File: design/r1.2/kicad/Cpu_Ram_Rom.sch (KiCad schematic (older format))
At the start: 19 parts, among them IC1 MC68010P10, IC4 MC68901P, J2 Conn_01x06, Q1 3.6864MHz, U1 AT28C256-15PU, U2 AT28C256-15PU, U3 AS6C4008-55PCN, U4 AS6C4008-55PCN

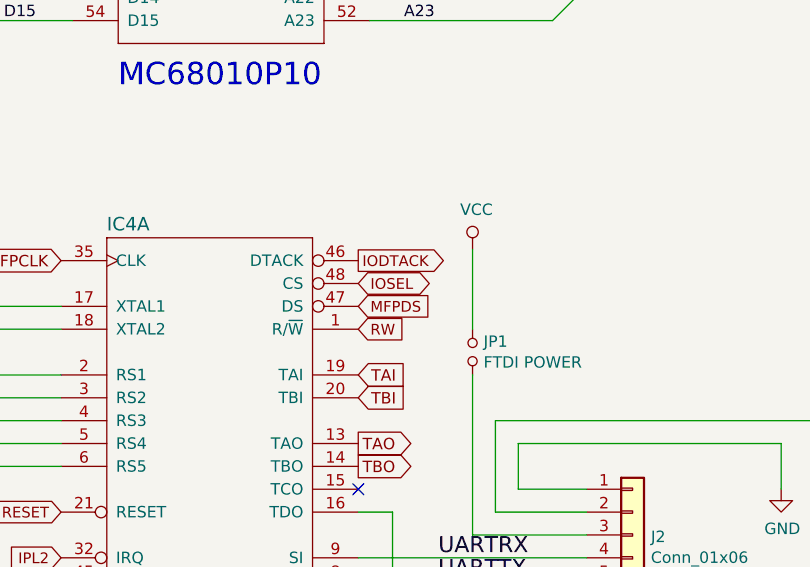
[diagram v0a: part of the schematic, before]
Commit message: More robust MFP decoding
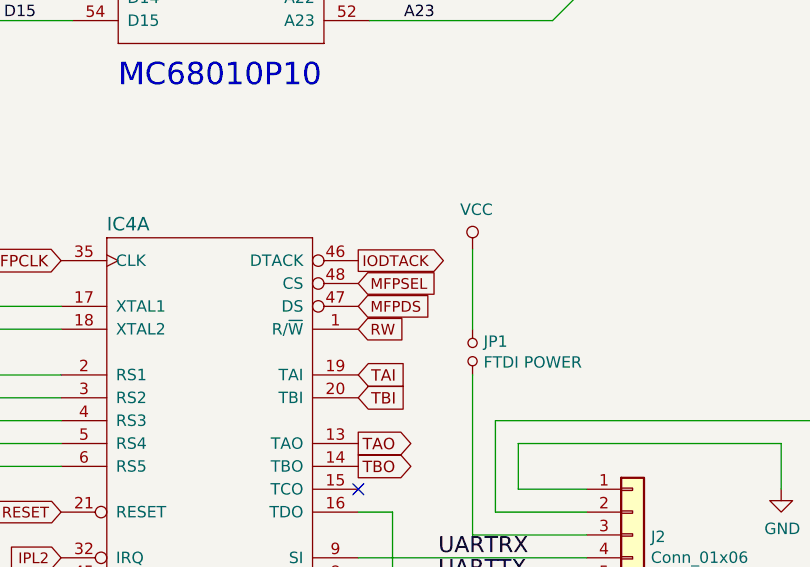
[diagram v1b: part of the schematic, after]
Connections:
- net IOSEL renamed MFPSEL
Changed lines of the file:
@@
 Text GLabel 4000 7550 0    47   Input ~ 0
 RESET
-Text GLabel 5300 6550 2    47   BiDi ~ 0
-IOSEL
+Text GLabel 5300 6550 2    47   Input ~ 0
+MFPSEL
 Wire Wire Line
 	1000 9100 1400 9100

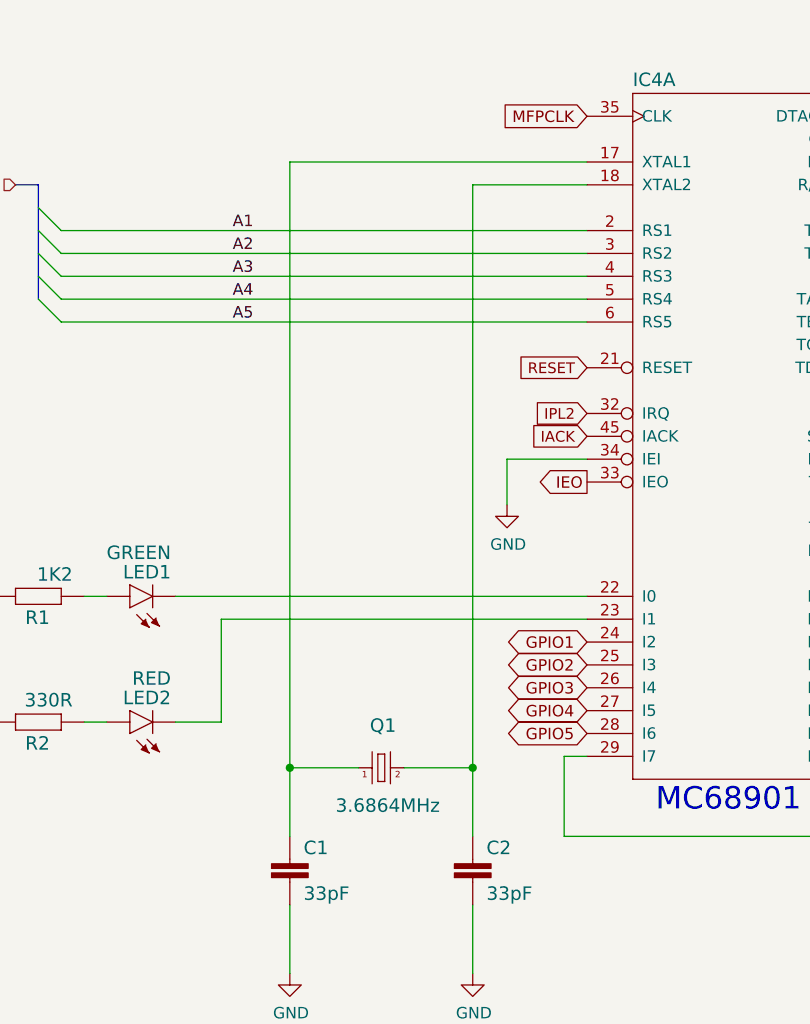
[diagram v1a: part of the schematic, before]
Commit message: Layout for 1.2 and PLD changes for same
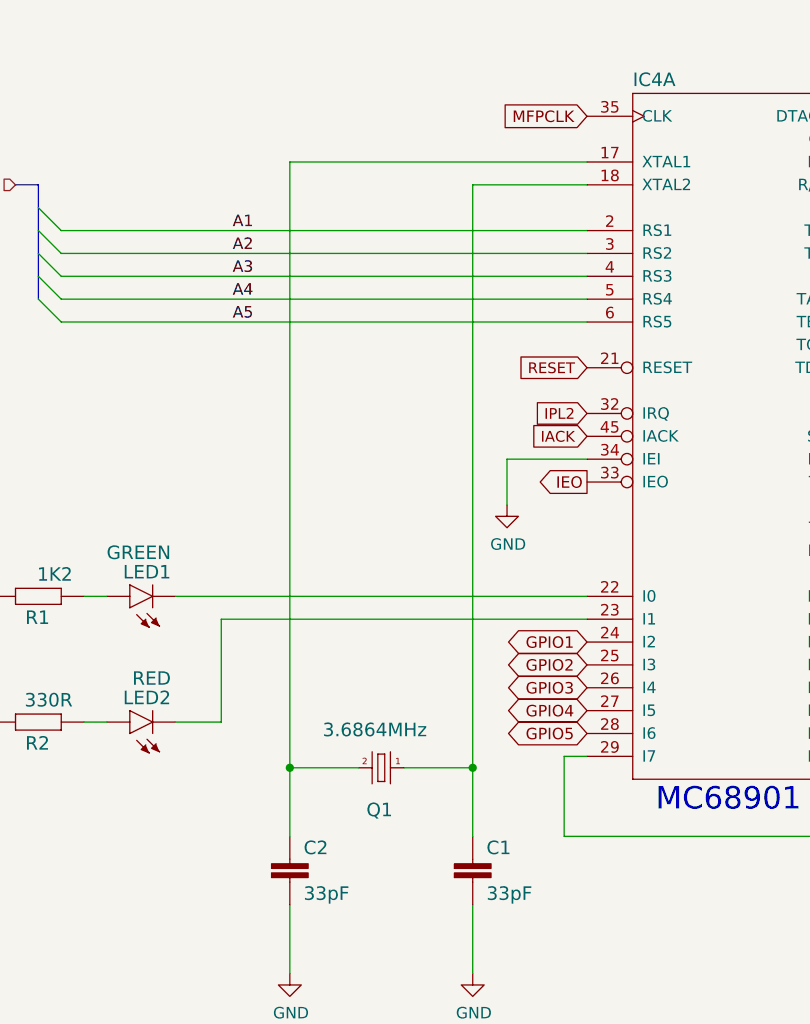
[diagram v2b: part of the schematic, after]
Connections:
- net at C1.1, Q1.1: now also IC4.18 (XTAL2); no longer IC4.17 (XTAL1)
- net at C2.1, Q1.2: now also IC4.17 (XTAL1); no longer IC4.18 (XTAL2)
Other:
- moved on the sheet: C1, C2
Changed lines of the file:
@@
 $EndComp
-Wire Wire Line
-	3000 9300 2700 9300
-Wire Wire Line
-	3200 9300 3500 9300
 Wire Wire Line
 	3650 7950 3650 8150
@@
 F 3 "" H 4700 7750 50  0001 C CNN
 	1    4700 7750
-	1    0    0    -1
-$EndComp
-$Comp
-L rosco_m68k-eagle-import:CRYSTALHC49S Q?
-U 1 1 5F15ED89
-P 3100 9300
-AR Path="/5F15ED89" Ref="Q?"  Part="1"
-AR Path="/5E53B630/5F15ED89" Ref="Q?"  Part="1"
-AR Path="/5E53B4B8/5F15ED89" Ref="Q1"  Part="1"
-F 0 "Q1" H 3050 9450 59  0000 L BNN
-F 1 "3.6864MHz" H 2900 9100 59  0000 L BNN
-F 2 "rosco_m68k:HC49_S" H 3100 9300 50  0001 C CNN
-F 3 "" H 3100 9300 50  0001 C CNN
-	1    3100 9300
 	1    0    0    -1
 $EndComp
@@
 L rosco_m68k-eagle-import:C2,5-3 C?
 U 1 1 5F15ED95
-P 3500 9700
+P 2700 9700
 AR Path="/5F15ED95" Ref="C?"  Part="1"
 AR Path="/5E53B630/5F15ED95" Ref="C?"  Part="1"
 AR Path="/5E53B4B8/5F15ED95" Ref="C2"  Part="1"
-F 0 "C2" H 3560 9715 59  0000 L BNN
+F 0 "C2" H 2760 9715 59  0000 L BNN
+F 1 "33pF" H 2760 9515 59  0000 L BNN
+F 2 "rosco_m68k:C2.5-3" H 2700 9700 50  0001 C CNN
+F 3 "" H 2700 9700 50  0001 C CNN
+	1    2700 9700
+	1    0    0    -1
+$EndComp
+$Comp
+L rosco_m68k-eagle-import:C2,5-3 C?
+U 1 1 5F15ED8F
+P 3500 9700
+AR Path="/5F15ED8F" Ref="C?"  Part="1"
+AR Path="/5E53B630/5F15ED8F" Ref="C?"  Part="1"
+AR Path="/5E53B4B8/5F15ED8F" Ref="C1"  Part="1"
+F 0 "C1" H 3560 9715 59  0000 L BNN
 F 1 "33pF" H 3560 9515 59  0000 L BNN
 F 2 "rosco_m68k:C2.5-3" H 3500 9700 50  0001 C CNN
@@
 	1    0    0    -1
 $EndComp
-$Comp
-L rosco_m68k-eagle-import:C2,5-3 C?
-U 1 1 5F15ED8F
-P 2700 9700
-AR Path="/5F15ED8F" Ref="C?"  Part="1"
-AR Path="/5E53B630/5F15ED8F" Ref="C?"  Part="1"
-AR Path="/5E53B4B8/5F15ED8F" Ref="C1"  Part="1"
-F 0 "C1" H 2760 9715 59  0000 L BNN
-F 1 "33pF" H 2760 9515 59  0000 L BNN
-F 2 "rosco_m68k:C2.5-3" H 2700 9700 50  0001 C CNN
-F 3 "" H 2700 9700 50  0001 C CNN
-	1    2700 9700
-	1    0    0    -1
-$EndComp
-Wire Wire Line
-	2700 9300 2700 9600
-Wire Wire Line
-	3500 9300 3500 9600
-Wire Wire Line
-	3500 9300 3500 6750
-Connection ~ 3500 9300
-Wire Wire Line
-	2700 9300 2700 6650
 Wire Wire Line
 	2700 6650 4000 6650
-Connection ~ 2700 9300
 Text GLabel 4000 6450 0    50   Input ~ 0
 MFPCLK
@@
 Wire Wire Line
 	15000 8750 15000 9250
+Wire Wire Line
+	2700 6650 2700 9300
+Wire Wire Line
+	3500 6750 3500 9300
+$Comp
+L rosco_m68k-eagle-import:CRYSTALHC49S Q?
+U 1 1 5F15ED89
+P 3100 9300
+AR Path="/5F15ED89" Ref="Q?"  Part="1"
+AR Path="/5E53B630/5F15ED89" Ref="Q?"  Part="1"
+AR Path="/5E53B4B8/5F15ED89" Ref="Q1"  Part="1"
+F 0 "Q1" H 3050 9450 59  0000 L BNN
+F 1 "3.6864MHz" H 2900 9100 59  0000 L BNN
+F 2 "rosco_m68k:HC49_S" H 3100 9300 50  0001 C CNN
+F 3 "" H 3100 9300 50  0001 C CNN
+	1    3100 9300
+	-1   0    0    1
+$EndComp
+Wire Wire Line
+	3000 9300 2700 9300
+Connection ~ 2700 9300
+Wire Wire Line
+	2700 9300 2700 9600
+Wire Wire Line
+	3200 9300 3500 9300
 Wire Bus Line
 	1600 6750 1600 7250
@@
 Wire Bus Line
 	15800 6550 15800 8450
+Connection ~ 3500 9300
+Wire Wire Line
+	3500 9300 3500 9600
 $EndSCHEMATC

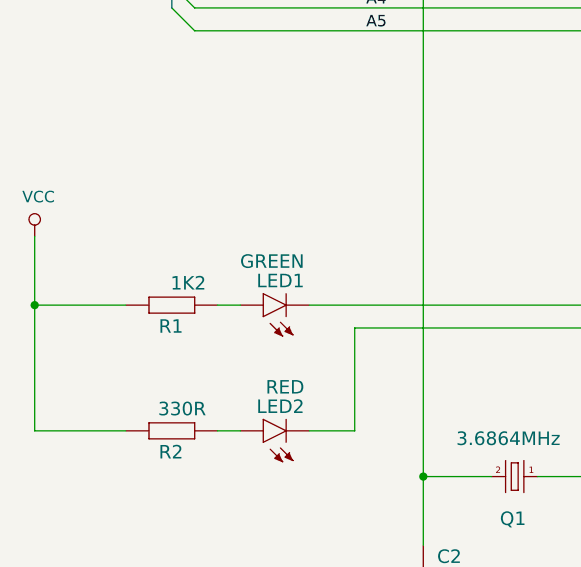
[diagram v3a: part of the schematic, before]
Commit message: Rerate LED limiters for new LED stock
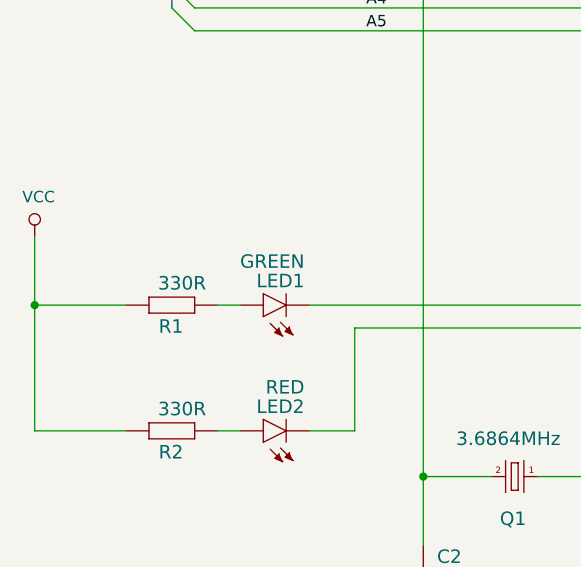
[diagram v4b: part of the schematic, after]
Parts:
- R1: value 1K2 -> 330R
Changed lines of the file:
@@
 AR Path="/5E53B4B8/5F15EDB1" Ref="R1"  Part="1"
 F 0 "R1" H 1550 8609 59  0000 L BNN
-F 1 "1K2" H 1450 8420 59  0000 L BNN
+F 1 "330R" H 1450 8420 59  0000 L BNN
 F 2 "rosco_m68k:0207_10" H 1600 8550 50  0001 C CNN
 F 3 "" H 1600 8550 50  0001 C CNN
